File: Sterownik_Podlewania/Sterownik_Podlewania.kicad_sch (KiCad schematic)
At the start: 27 parts, among them J1 Conn_01x06_Socket, J2 Conn_01x06_Socket, J3 RJ45, J4 Conn_01x04_Socket, J5 RJ45, J6 RJ45, J7 Conn_01x05_Socket, J8 RJ45, U1 ESP32-DEVKITC

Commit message: Dodanie footprintów schotky, kondesatorów
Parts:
- D21: footprint (none) -> Diode_SMD:D_SOD-123
- J4: footprint Connector_Harwin:Harwin_M20-89006xx_1x06_P2.54mm_Horizontal -> Connector_Harwin:Harwin_M20-89004xx_1x04_P2.54mm_Horizontal
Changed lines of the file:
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@@
 		(polyline
 			(pts
-				(xy 283.2497 81.28) (xy 283.21 165.1) (xy 176.6887 165.1) (xy 176.4903 81.28)
+				(xy 283.2496 92.71) (xy 283.21 165.1) (xy 176.6887 165.1) (xy 176.4902 92.71)
 			)
 			(stroke
@@
 			)
 		)
-		(property "Footprint" "Connector_Harwin:Harwin_M20-89006xx_1x06_P2.54mm_Horizontal"
+		(property "Footprint" "Connector_Harwin:Harwin_M20-89004xx_1x04_P2.54mm_Horizontal"
 			(at 147.32 127 0)
 			(effects
@@
 			)
 		)
-		(property "Footprint" ""
+		(property "Footprint" "Diode_SMD:D_SOD-123"
 			(at 59.69 36.83 0)
 			(effects

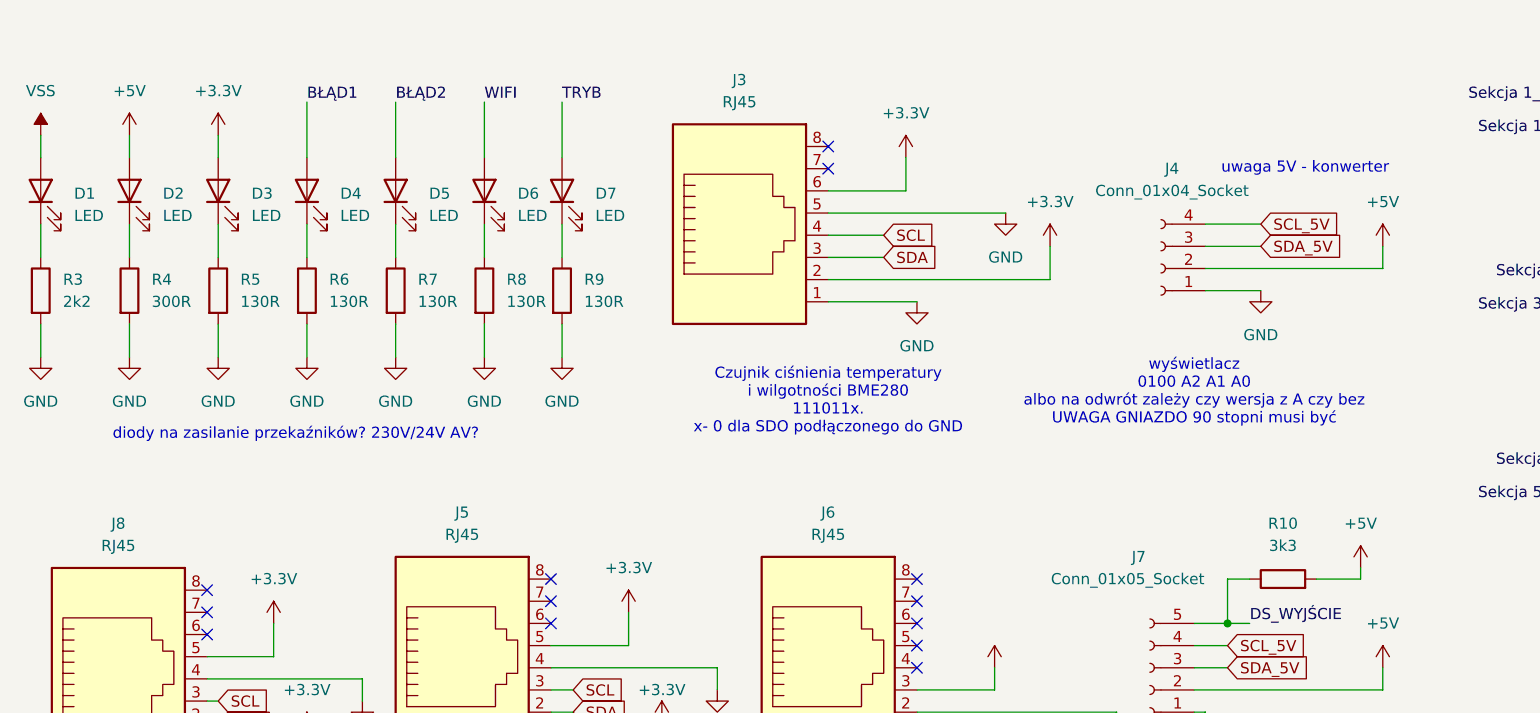
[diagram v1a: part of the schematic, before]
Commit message: Dodanie modeli 3d, nowy footprint do przełącznika, przerzucenie na drugą stronę płytki elementów, wstępne rozdzielenie elemntów pasywnych
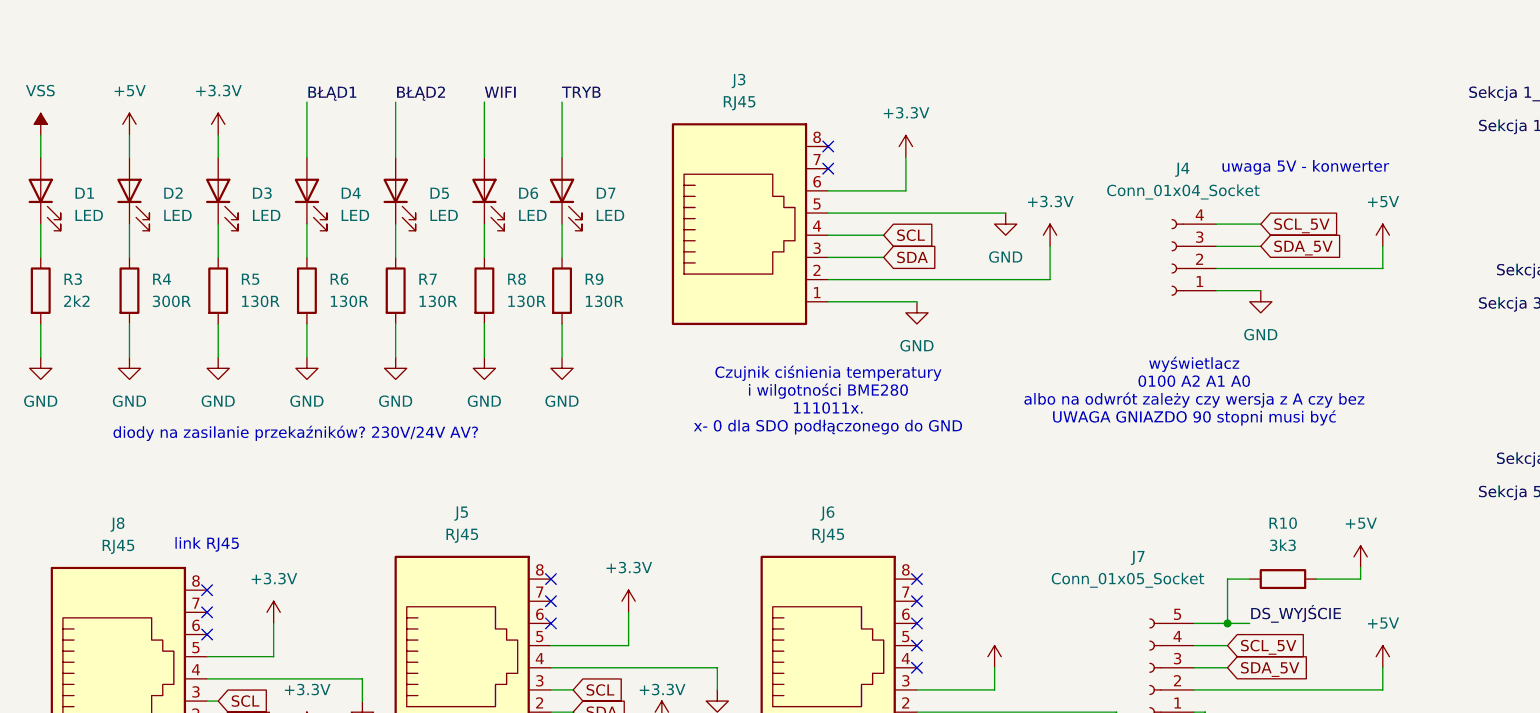
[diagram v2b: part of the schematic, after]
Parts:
- J1, J2: footprint Connector_Harwin:Harwin_M20-89006xx_1x06_P2.54mm_Horizontal -> Connector_PinHeader_2.54mm:PinHeader_1x06_P2.54mm_Vertical
- J4: footprint Connector_Harwin:Harwin_M20-89004xx_1x04_P2.54mm_Horizontal -> Connector_PinHeader_2.54mm:PinHeader_1x04_P2.54mm_Vertical
- J7: footprint Connector_Harwin:Harwin_M20-89005xx_1x05_P2.54mm_Horizontal -> Connector_PinHeader_2.54mm:PinHeader_1x05_P2.54mm_Vertical
- U1: footprint RF_Module:ESP32-C3-DevKitM-1 -> ESP32:MODULE_ESP32-DEVKITC
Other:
- note added: "link RJ45"
- moved on the sheet: J4
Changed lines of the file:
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@@
 		)
 	)
+	(text "link RJ45"
+		(exclude_from_sim no)
+		(at 38.1 158.75 0)
+		(effects
+			(font
+				(size 1.27 1.27)
+			)
+			(href "https://www.tme.eu/pl/details/mj3215-88-1-2-n/zlacza-rj/gct/")
+		)
+	)
 	(text "wyświetlacz\n0100 A2 A1 A0 \nalbo na odwrót zależy czy wersja z A czy bez\nUWAGA GNIAZDO 90 stopni musi być\n\n"
 		(exclude_from_sim no)
@@
 	(wire
 		(pts
-			(xy 152.4 127) (xy 172.72 127)
+			(xy 153.67 127) (xy 172.72 127)
 		)
 		(stroke
@@
 	(wire
 		(pts
-			(xy 172.72 124.46) (xy 172.72 127)
+			(xy 172.72 127) (xy 172.72 124.46)
 		)
 		(stroke
@@
 	(wire
 		(pts
-			(xy 152.4 129.54) (xy 158.75 129.54)
+			(xy 153.67 129.54) (xy 158.75 129.54)
 		)
 		(stroke
@@
 	(wire
 		(pts
-			(xy 152.4 124.46) (xy 158.75 124.46)
+			(xy 153.67 124.46) (xy 158.75 124.46)
 		)
 		(stroke
@@
 	(wire
 		(pts
-			(xy 152.4 121.92) (xy 158.75 121.92)
+			(xy 153.67 121.92) (xy 158.75 121.92)
 		)
 		(stroke
@@
 			)
 		)
-		(property "Footprint" "Connector_Harwin:Harwin_M20-89006xx_1x06_P2.54mm_Horizontal"
+		(property "Footprint" "Connector_PinHeader_2.54mm:PinHeader_1x06_P2.54mm_Vertical"
 			(at 275.59 63.5 0)
 			(effects
@@
 			)
 		)
-		(property "Footprint" "Connector_Harwin:Harwin_M20-89005xx_1x05_P2.54mm_Horizontal"
+		(property "Footprint" "Connector_PinHeader_2.54mm:PinHeader_1x05_P2.54mm_Vertical"
 			(at 146.05 172.72 0)
 			(effects
@@
 	(symbol
 		(lib_id "Connector:Conn_01x04_Socket")
-		(at 147.32 127 180)
+		(at 148.59 127 180)
 		(unit 1)
 		(exclude_from_sim no)
@@
 		(dnp no)
 		(property "Reference" "J4"
-			(at 148.59 115.57 0)
+			(at 149.86 115.57 0)
 			(effects
 				(font
@@
 		)
 		(property "Value" "Conn_01x04_Socket"
-			(at 148.59 118.11 0)
+			(at 149.86 118.11 0)
 			(effects
 				(font
@@
 			)
 		)
-		(property "Footprint" "Connector_Harwin:Harwin_M20-89004xx_1x04_P2.54mm_Horizontal"
-			(at 147.32 127 0)
+		(property "Footprint" "Connector_PinHeader_2.54mm:PinHeader_1x04_P2.54mm_Vertical"
+			(at 148.59 127 0)
 			(effects
 				(font
@@
 		)
 		(property "Datasheet" "~"
-			(at 147.32 127 0)
+			(at 148.59 127 0)
 			(effects
 				(font
@@
 		)
 		(property "Description" "Generic connector, single row, 01x04, script generated"
-			(at 147.32 127 0)
+			(at 148.59 127 0)
 			(effects
 				(font
@@
 			)
 		)
-		(property "Footprint" "RF_Module:ESP32-C3-DevKitM-1"
+		(property "Footprint" "ESP32:MODULE_ESP32-DEVKITC"
 			(at 85.09 59.69 0)
 			(effects
@@
 			)
 		)
-		(property "Footprint" "Connector_Harwin:Harwin_M20-89006xx_1x06_P2.54mm_Horizontal"
+		(property "Footprint" "Connector_PinHeader_2.54mm:PinHeader_1x06_P2.54mm_Vertical"
 			(at 275.59 40.64 0)
 			(effects

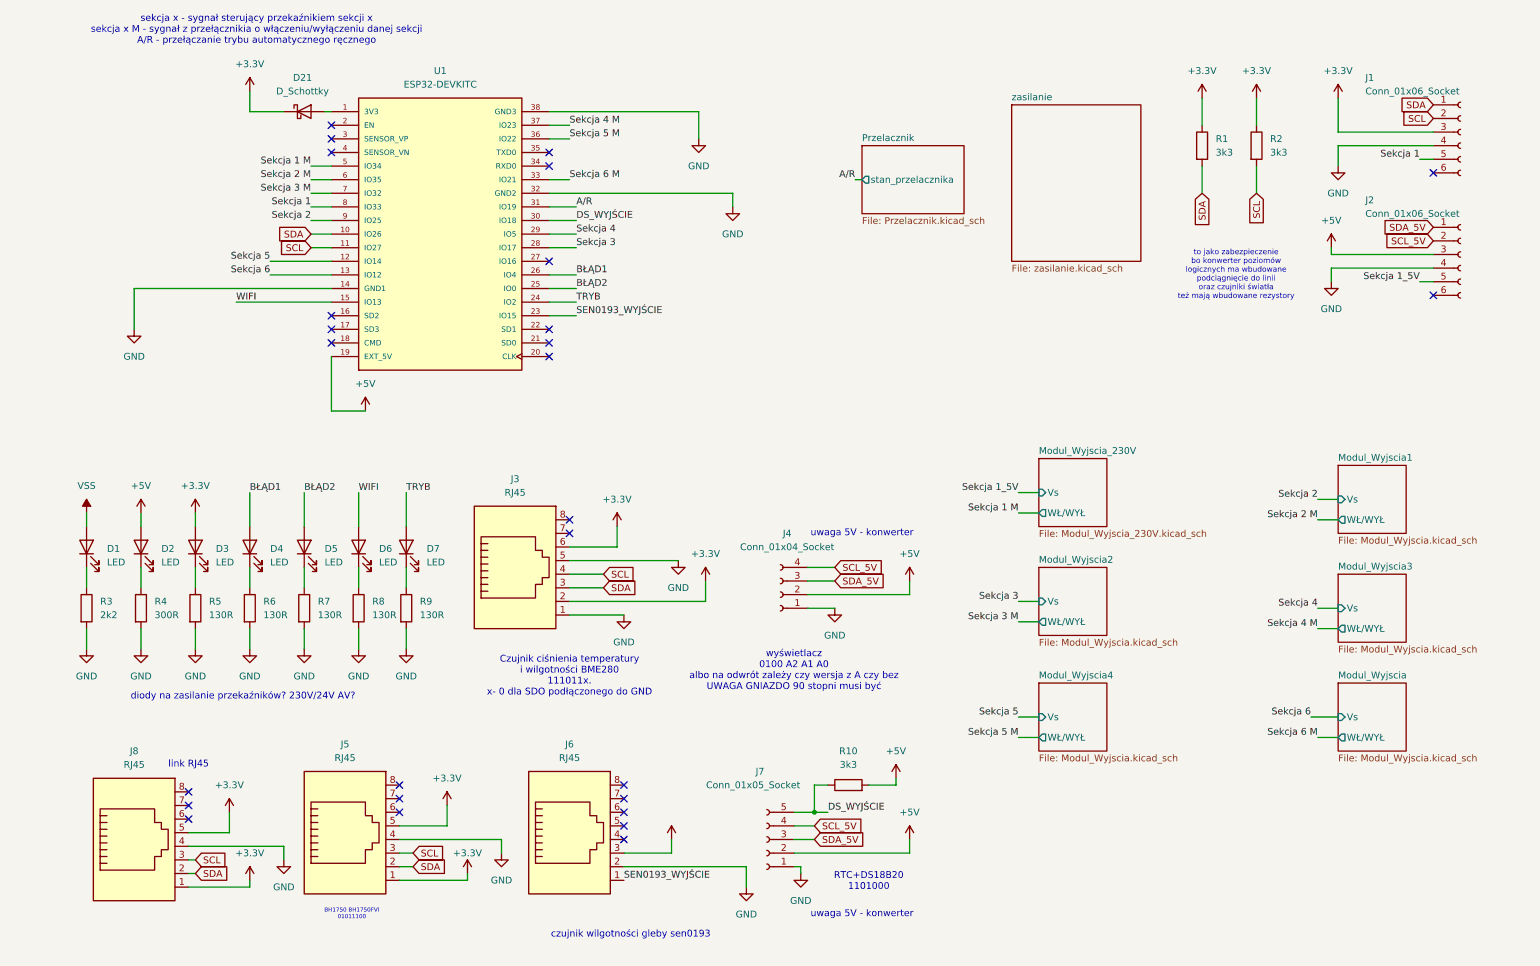
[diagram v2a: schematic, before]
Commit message: dodanie modeli 3d, poprawa footprintu RTC
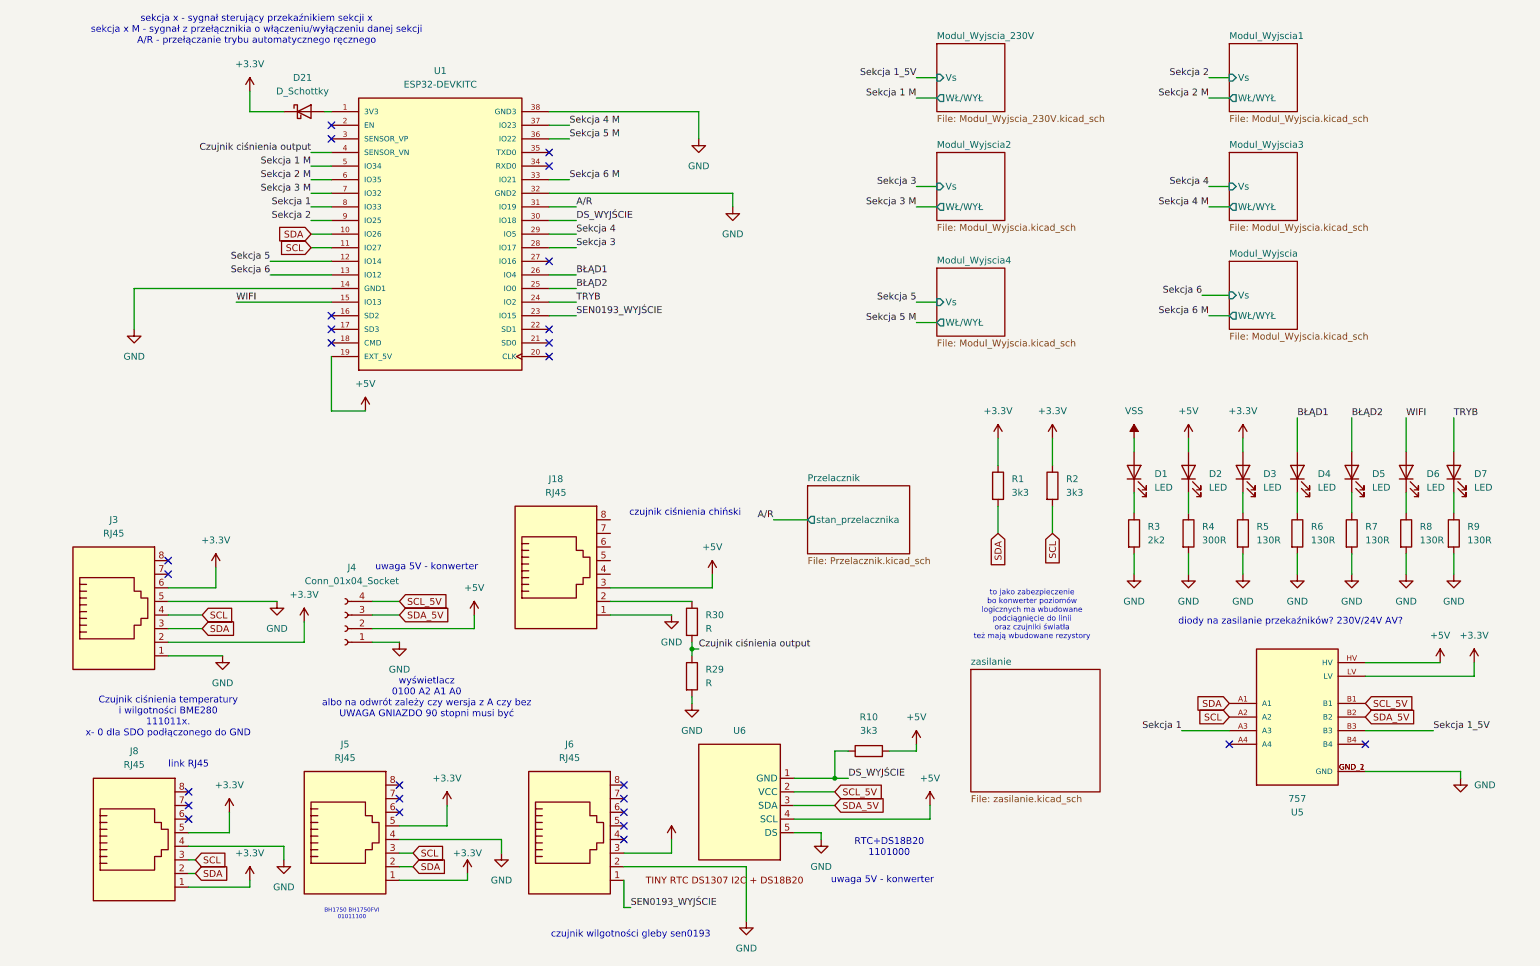
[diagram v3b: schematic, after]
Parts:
- removed J1, J2: Conn_01x06_Socket, Connector_PinHeader_2.54mm:PinHeader_1x06_P2.54mm_Vertical, symbol Connector:Conn_01x06_Socket
- removed J7: Conn_01x05_Socket, Connector_PinHeader_2.54mm:PinHeader_1x05_P2.54mm_Vertical, symbol Connector:Conn_01x05_Socket
- added J18: RJ45, Connector_RJ:RJ45_Amphenol_54602-x08_Horizontal, symbol Connector:RJ45
- added R29, R30: R, Resistor_SMD:R_1206_3216Metric, symbol Device:R
- added U5: 757, Voltage_Level_Converters:MODULE_757, symbol Voltage_Level_Converter:757
- added U6: ~, RTC:RTC DS1307 + 32kb EEPROM 24C32 I2C, symbol RTC:TINY_RTC_DS1307
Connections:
- net +3.3V: now also U5.LV
- net +5V: now also J18.3, U5.HV, U6.4 (SCL)
- net DS_WYJŚCIE: now also U6.1 (GND)
- net GND: now also J18.1, R29.2, U5.GND_1 (GND), U5.GND_2 (GND), U6.5 (DS)
- net SCL: now also U5.A2
- net SCL_5V: now also U5.B1, U6.2 (VCC)
- net SDA: now also U5.A1
- net SDA_5V: now also U5.B2, U6.3 (SDA)
- net Sekcja 1: now also U5.A3
- net Sekcja 1_5V: now also U5.B3
- net Czujnik ciśnienia output: now reaches U1.4 (SENSOR_VN)
- net Czujnik ciśnienia output: now also R29.1, R30.2
- new net: J18.2, R30.1
- no-connect marks 27 -> 26
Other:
- note added: "czujnik ciśnienia chiński"
- moved on the sheet: D1, D2, D3, D4, D5, D6, D7, J3, J4, R1, R10, R2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

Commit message: Wstępny finalny rozkład płytki, narysowanie outlinu
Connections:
- net SEN0193_WYJŚCIE: now also U1.15 (IO13); no longer U1.23 (IO15)
- net TRYB: now also U1.23 (IO15); no longer U1.24 (IO2)
- net WIFI: now also U1.24 (IO2); no longer U1.15 (IO13)
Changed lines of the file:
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@@
+	(wire
+		(pts
+			(xy 105.41 74.93) (xy 110.49 74.93)
+		)
+		(stroke
+			(width 0)
+			(type default)
+		)
+	)
 	(wire
 		(pts
@@
 	(wire
 		(pts
-			(xy 105.41 74.93) (xy 110.49 74.93)
-		)
-		(stroke
-			(width 0)
-			(type default)
-		)
-	)
-	(wire
-		(pts
 			(xy 158.75 163.83) (xy 151.13 163.83)
 		)
@@
 	(wire
 		(pts
-			(xy 46.99 72.39) (xy 64.77 72.39)
-		)
-		(stroke
-			(width 0)
-			(type default)
-		)
-	)
-	(wire
-		(pts
 			(xy 173.99 30.48) (xy 177.8 30.48)
 		)
@@
 		(pts
 			(xy 49.53 36.83) (xy 49.53 33.02)
+		)
+		(stroke
+			(width 0)
+			(type default)
+		)
+	)
+	(wire
+		(pts
+			(xy 64.77 72.39) (xy 54.61 72.39)
 		)
 		(stroke
@@
 		)
 	)
-	(label "SEN0193_WYJŚCIE"
+	(label "TRYB"
 		(at 110.49 74.93 0)
 		(effects
@@
 		)
 	)
+	(label "SEN0193_WYJŚCIE"
+		(at 54.61 72.39 180)
+		(effects
+			(font
+				(size 1.27 1.27)
+			)
+			(justify right bottom)
+		)
+	)
 	(label "Sekcja 4"
 		(at 110.49 59.69 0)
@@
 		)
 	)
-	(label "WIFI"
-		(at 46.99 72.39 0)
-		(effects
-			(font
-				(size 1.27 1.27)
-			)
-			(justify left bottom)
-		)
-	)
-	(label "TRYB"
-		(at 110.49 72.39 0)
-		(effects
-			(font
-				(size 1.27 1.27)
-			)
-			(justify left bottom)
-		)
-	)
 	(label "Sekcja 1_5V"
 		(at 270.51 152.4 0)
@@
 		(effects
 			(font
+				(size 1.27 1.27)
+			)
+			(justify left bottom)
+		)
+	)
+	(label "WIFI"
+		(at 110.49 72.39 0)
+		(effects
+			(font
